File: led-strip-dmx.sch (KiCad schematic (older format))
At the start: 35 parts, among them IC1 ATMEGA168-P, IC2 MAX485, IC3 74HC165, P1 POWER_IN, P2 POWER_OUT, P3 ISP, P4 LED_OUT, P5 SIGNAL_IN, P6 SIGNAL_OUT, Q1 IRF640N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

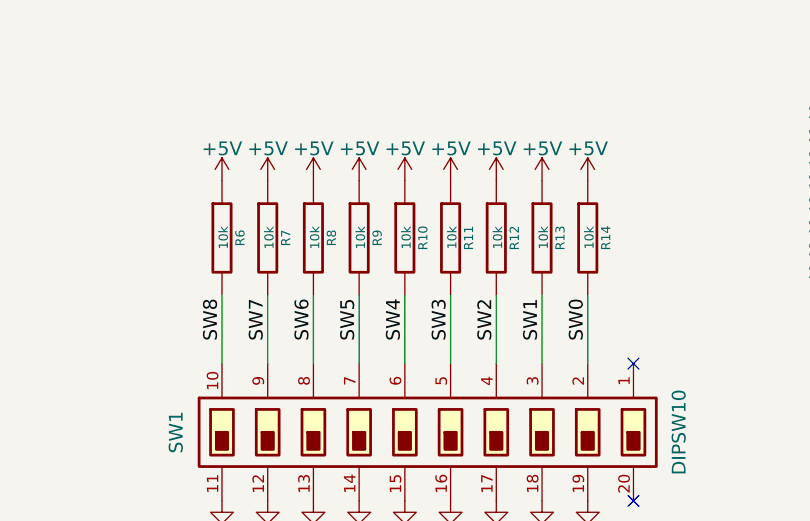
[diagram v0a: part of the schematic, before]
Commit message: Fix a few major issues on the PCB
- Used wrong pin order for LED transistors
- Right half of the PCB did not get any power
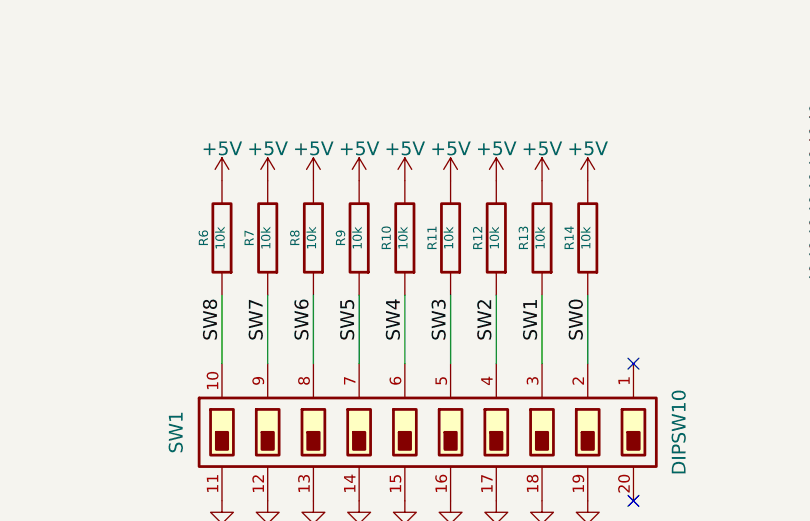
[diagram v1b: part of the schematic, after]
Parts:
- R1, R10, R11, R12, R13, R14, R2, R3, R4, R5, R6, R7, R8, R9: footprint Resistors_ThroughHole:Resistor_Horizontal_RM15mm -> Resistors_ThroughHole:Resistor_Horizontal_RM10mm
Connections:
- net +5V: now also R10.2, R11.2, R12.2, R13.2, R14.2, R6.2, R7.2, R8.2, R9.2; no longer R10.1, R11.1, R12.1, R13.1, R14.1, R6.1, R7.1, R8.1, R9.1
- net SW0: now also R14.1; no longer R14.2
- net SW1: now also R13.1; no longer R13.2
- net SW2: now also R12.1; no longer R12.2
- net SW3: now also R11.1; no longer R11.2
- net SW4: now also R10.1; no longer R10.2
- net SW5: now also R9.1; no longer R9.2
- net SW6: now also R8.1; no longer R8.2
- net SW7: now also R7.1; no longer R7.2
- net SW8: now also R6.1; no longer R6.2
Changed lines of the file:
@@
 F 0 "R4" V 5880 3650 40  0000 C CNN
 F 1 "10k" V 5807 3651 40  0000 C CNN
-F 2 "Resistors_ThroughHole:Resistor_Horizontal_RM15mm" V 5730 3650 30  0001 C CNN
+F 2 "Resistors_ThroughHole:Resistor_Horizontal_RM10mm" V 5730 3650 30  0001 C CNN
 F 3 "" H 5800 3650 30  0000 C CNN
 	1    5800 3650
@@
 F 0 "R5" V 6480 4350 40  0000 C CNN
 F 1 "10k" V 6407 4351 40  0000 C CNN
-F 2 "Resistors_ThroughHole:Resistor_Horizontal_RM15mm" V 6330 4350 30  0001 C CNN
+F 2 "Resistors_ThroughHole:Resistor_Horizontal_RM10mm" V 6330 4350 30  0001 C CNN
 F 3 "" H 6400 4350 30  0000 C CNN
 	1    6400 4350
@@
 F 0 "R1" V 2580 6150 40  0000 C CNN
 F 1 "680" V 2507 6151 40  0000 C CNN
-F 2 "Resistors_ThroughHole:Resistor_Horizontal_RM15mm" V 2430 6150 30  0001 C CNN
+F 2 "Resistors_ThroughHole:Resistor_Horizontal_RM10mm" V 2430 6150 30  0001 C CNN
 F 3 "" H 2500 6150 30  0000 C CNN
 	1    2500 6150
@@
 F 0 "R2" V 3380 6150 40  0000 C CNN
 F 1 "680" V 3307 6151 40  0000 C CNN
-F 2 "Resistors_ThroughHole:Resistor_Horizontal_RM15mm" V 3230 6150 30  0001 C CNN
+F 2 "Resistors_ThroughHole:Resistor_Horizontal_RM10mm" V 3230 6150 30  0001 C CNN
 F 3 "" H 3300 6150 30  0000 C CNN
 	1    3300 6150
@@
 F 0 "R3" V 4180 6150 40  0000 C CNN
 F 1 "680" V 4107 6151 40  0000 C CNN
-F 2 "Resistors_ThroughHole:Resistor_Horizontal_RM15mm" V 4030 6150 30  0001 C CNN
+F 2 "Resistors_ThroughHole:Resistor_Horizontal_RM10mm" V 4030 6150 30  0001 C CNN
 F 3 "" H 4100 6150 30  0000 C CNN
 	1    4100 6150
@@
 F 0 "R6" V 6830 1500 40  0000 C CNN
 F 1 "10k" V 6757 1501 40  0000 C CNN
-F 2 "Resistors_ThroughHole:Resistor_Horizontal_RM15mm" V 6680 1500 30  0001 C CNN
+F 2 "Resistors_ThroughHole:Resistor_Horizontal_RM10mm" V 6680 1500 30  0001 C CNN
 F 3 "" H 6750 1500 30  0000 C CNN
 	1    6750 1500
-	1    0    0    -1
+	-1   0    0    1
 $EndComp
 $Comp
@@
 F 0 "R7" V 7030 1500 40  0000 C CNN
 F 1 "10k" V 6957 1501 40  0000 C CNN
-F 2 "Resistors_ThroughHole:Resistor_Horizontal_RM15mm" V 6880 1500 30  0001 C CNN
+F 2 "Resistors_ThroughHole:Resistor_Horizontal_RM10mm" V 6880 1500 30  0001 C CNN
 F 3 "" H 6950 1500 30  0000 C CNN
 	1    6950 1500
-	1    0    0    -1
+	-1   0    0    1
 $EndComp
 $Comp
@@
 F 0 "R8" V 7230 1500 40  0000 C CNN
 F 1 "10k" V 7157 1501 40  0000 C CNN
-F 2 "Resistors_ThroughHole:Resistor_Horizontal_RM15mm" V 7080 1500 30  0001 C CNN
+F 2 "Resistors_ThroughHole:Resistor_Horizontal_RM10mm" V 7080 1500 30  0001 C CNN
 F 3 "" H 7150 1500 30  0000 C CNN
 	1    7150 1500
-	1    0    0    -1
+	-1   0    0    1
 $EndComp
 $Comp
@@
 F 0 "R9" V 7430 1500 40  0000 C CNN
 F 1 "10k" V 7357 1501 40  0000 C CNN
-F 2 "Resistors_ThroughHole:Resistor_Horizontal_RM15mm" V 7280 1500 30  0001 C CNN
+F 2 "Resistors_ThroughHole:Resistor_Horizontal_RM10mm" V 7280 1500 30  0001 C CNN
 F 3 "" H 7350 1500 30  0000 C CNN
 	1    7350 1500
-	1    0    0    -1
+	-1   0    0    1
 $EndComp
 $Comp
@@
 F 0 "R10" V 7630 1500 40  0000 C CNN
 F 1 "10k" V 7557 1501 40  0000 C CNN
-F 2 "Resistors_ThroughHole:Resistor_Horizontal_RM15mm" V 7480 1500 30  0001 C CNN
+F 2 "Resistors_ThroughHole:Resistor_Horizontal_RM10mm" V 7480 1500 30  0001 C CNN
 F 3 "" H 7550 1500 30  0000 C CNN
 	1    7550 1500
-	1    0    0    -1
+	-1   0    0    1
 $EndComp
 $Comp
@@
 F 0 "R11" V 7830 1500 40  0000 C CNN
 F 1 "10k" V 7757 1501 40  0000 C CNN
-F 2 "Resistors_ThroughHole:Resistor_Horizontal_RM15mm" V 7680 1500 30  0001 C CNN
+F 2 "Resistors_ThroughHole:Resistor_Horizontal_RM10mm" V 7680 1500 30  0001 C CNN
 F 3 "" H 7750 1500 30  0000 C CNN
 	1    7750 1500
-	1    0    0    -1
+	-1   0    0    1
 $EndComp
 $Comp
@@
 F 0 "R12" V 8030 1500 40  0000 C CNN
 F 1 "10k" V 7957 1501 40  0000 C CNN
-F 2 "Resistors_ThroughHole:Resistor_Horizontal_RM15mm" V 7880 1500 30  0001 C CNN
+F 2 "Resistors_ThroughHole:Resistor_Horizontal_RM10mm" V 7880 1500 30  0001 C CNN
 F 3 "" H 7950 1500 30  0000 C CNN
 	1    7950 1500
-	1    0    0    -1
+	-1   0    0    1
 $EndComp
 $Comp
@@
 F 0 "R13" V 8230 1500 40  0000 C CNN
 F 1 "10k" V 8157 1501 40  0000 C CNN
-F 2 "Resistors_ThroughHole:Resistor_Horizontal_RM15mm" V 8080 1500 30  0001 C CNN
+F 2 "Resistors_ThroughHole:Resistor_Horizontal_RM10mm" V 8080 1500 30  0001 C CNN
 F 3 "" H 8150 1500 30  0000 C CNN
 	1    8150 1500
-	1    0    0    -1
+	-1   0    0    1
 $EndComp
 $Comp
@@
 F 0 "R14" V 8430 1500 40  0000 C CNN
 F 1 "10k" V 8357 1501 40  0000 C CNN
-F 2 "Resistors_ThroughHole:Resistor_Horizontal_RM15mm" V 8280 1500 30  0001 C CNN
+F 2 "Resistors_ThroughHole:Resistor_Horizontal_RM10mm" V 8280 1500 30  0001 C CNN
 F 3 "" H 8350 1500 30  0000 C CNN
 	1    8350 1500
-	1    0    0    -1
-$EndComp
-$Comp
+	-1   0    0    1
+$EndComp
+$Comp
